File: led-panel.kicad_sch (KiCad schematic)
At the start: 0 parts

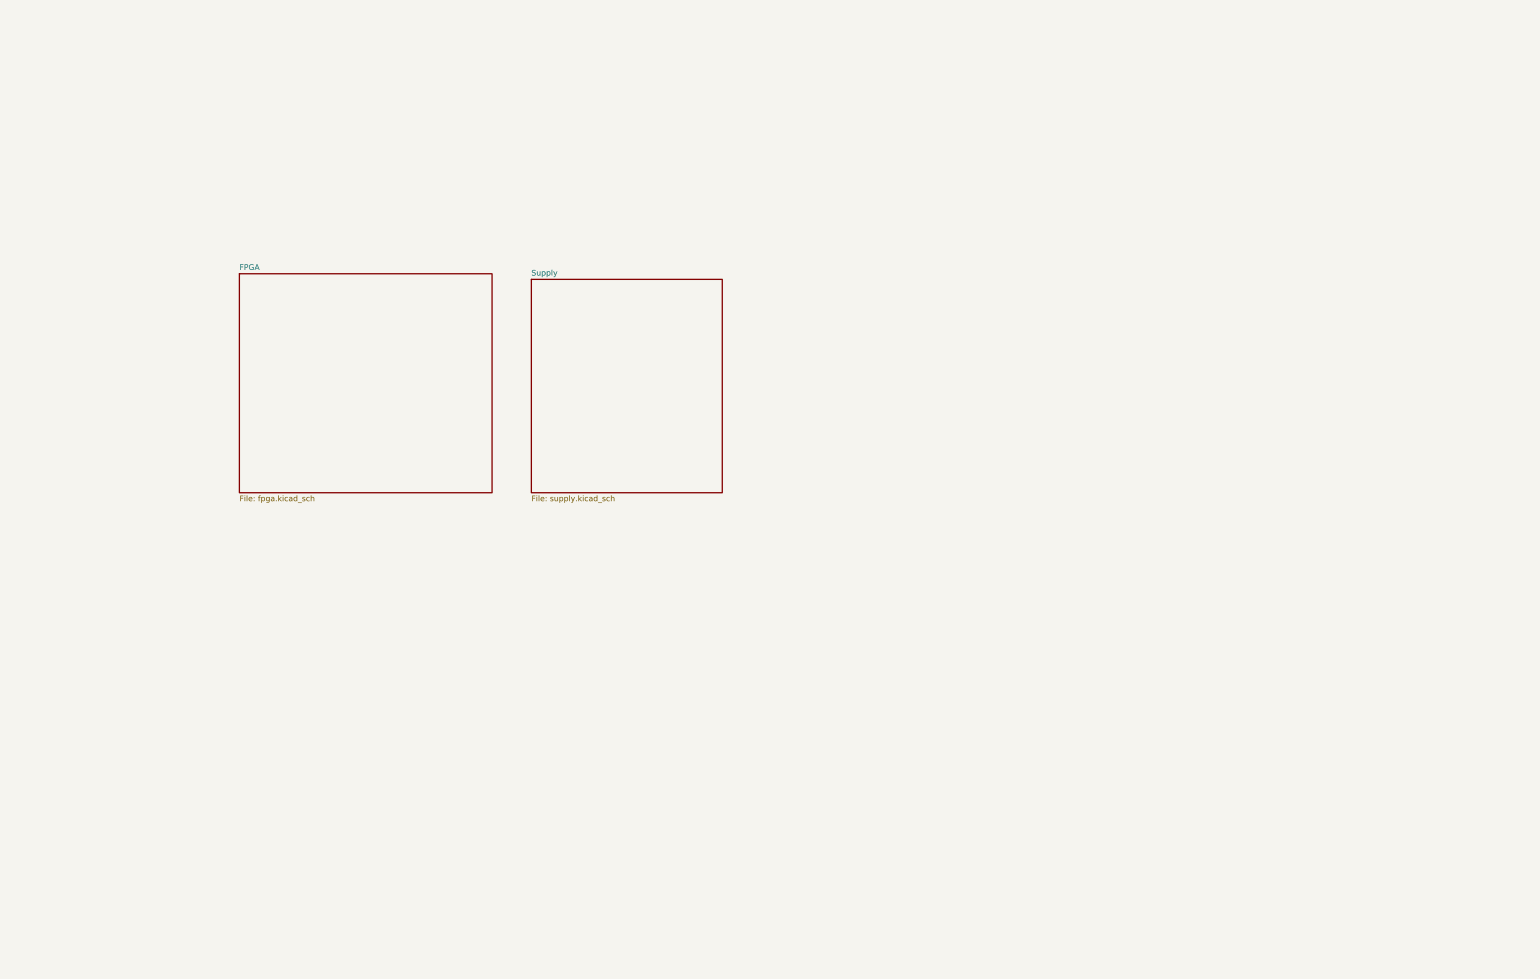
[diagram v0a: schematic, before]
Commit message: [#72133] Add rough schematic hierarchy
Signed-off-by: Dawid Lentka <dlentka@antmicro.com>
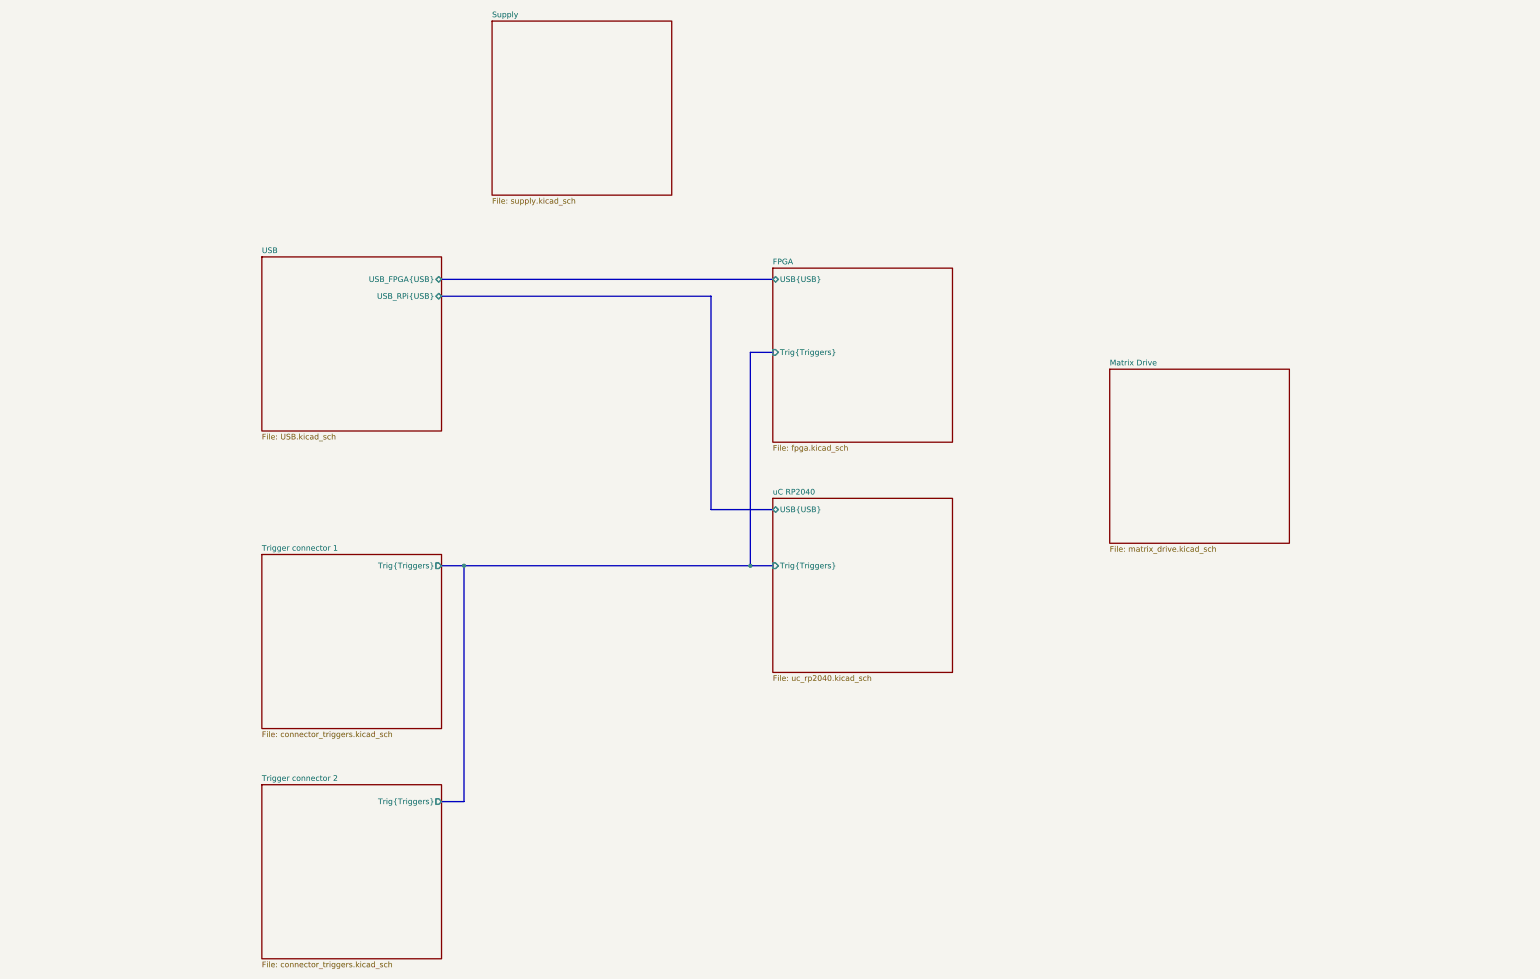
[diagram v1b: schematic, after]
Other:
- added sheet Matrix Drive (matrix_drive.kicad_sch)
- added sheet Trigger connector 1 (connector_triggers.kicad_sch)
- added sheet Trigger connector 2 (connector_triggers.kicad_sch)
- added sheet USB (USB.kicad_sch)
- added sheet uC RP2040 (uc_rp2040.kicad_sch)
- sheet FPGA ports: added Trig{Triggers}, USB{USB}; removed none

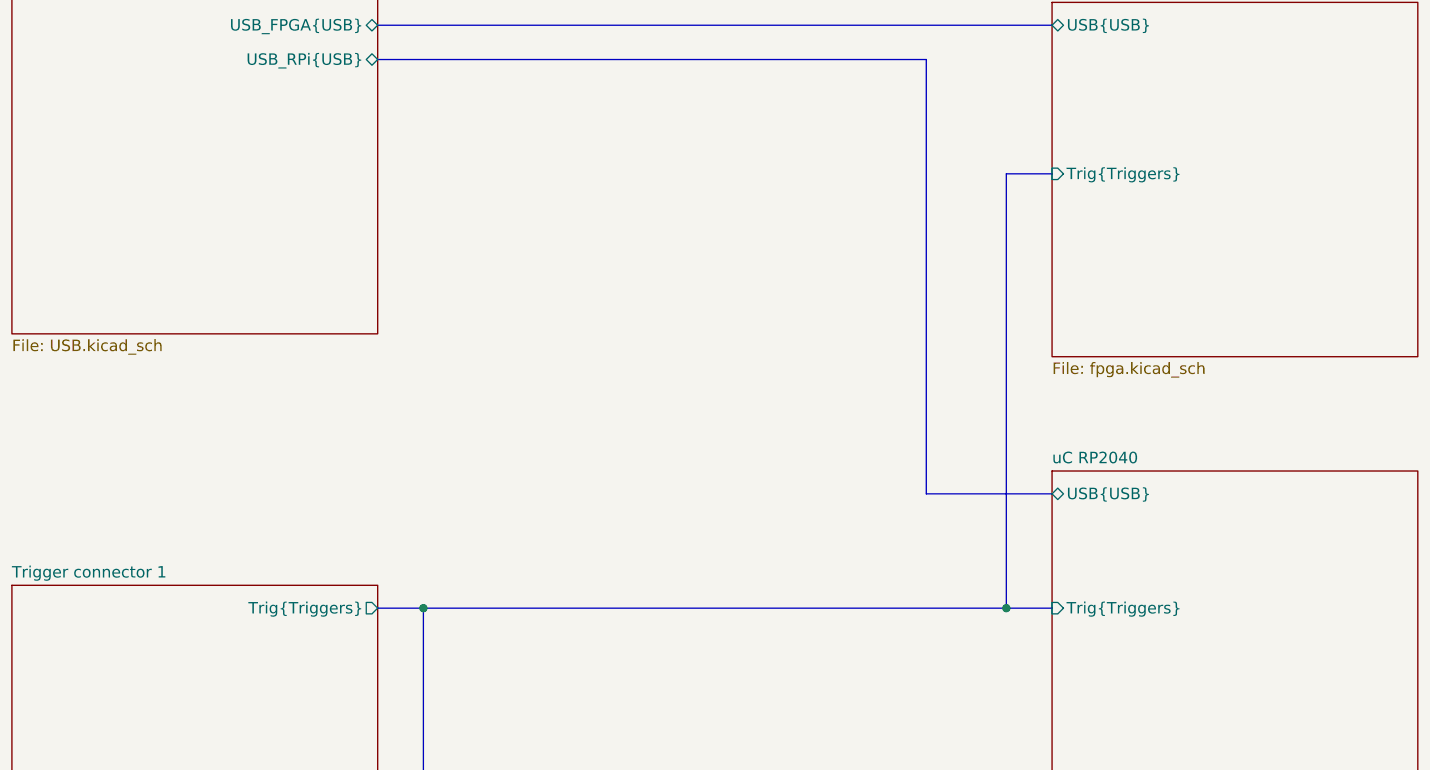
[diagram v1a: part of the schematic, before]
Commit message: [#72133] Add USB mux
Signed-off-by: Dawid Lentka <dlentka@antmicro.com>
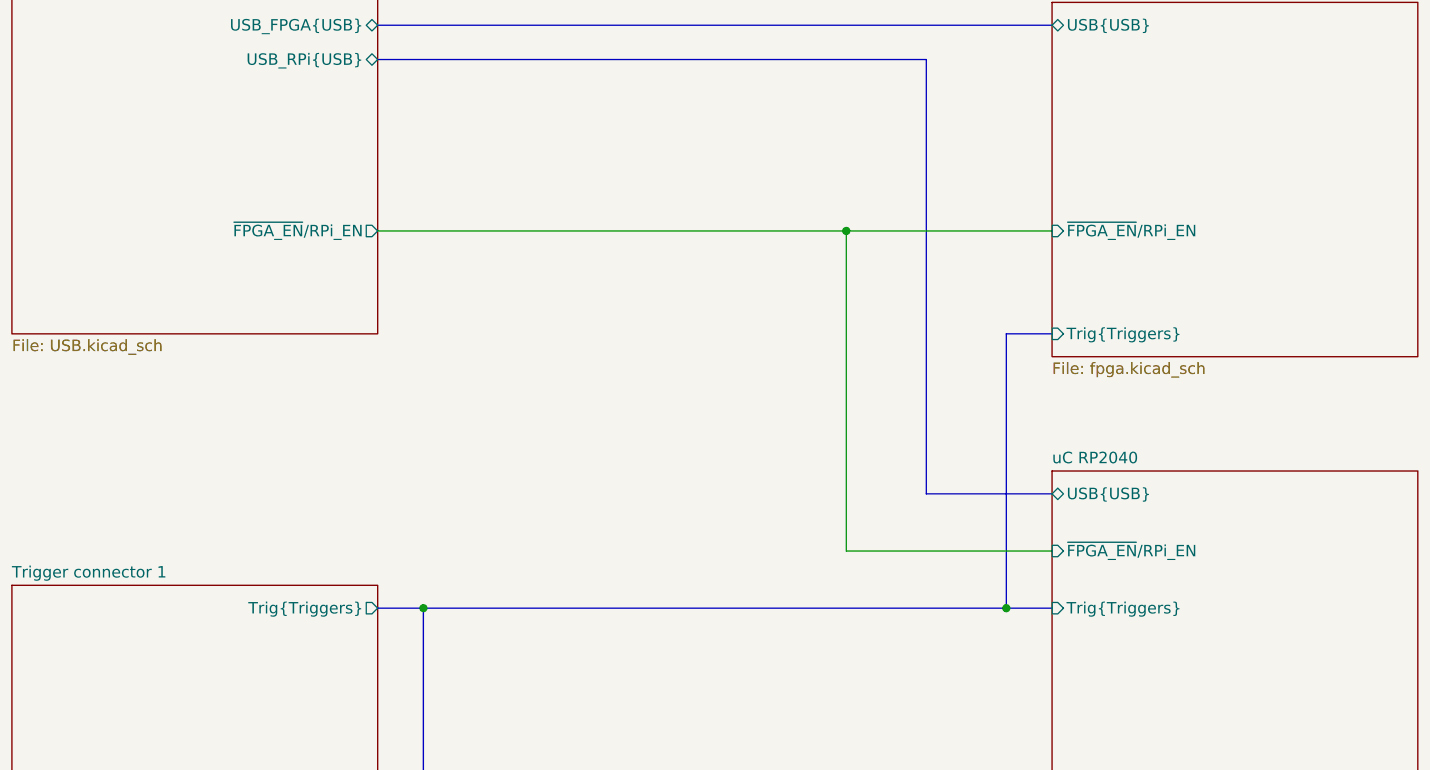
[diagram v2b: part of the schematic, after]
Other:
- sheet FPGA ports: added ~{FPGA_EN}/RPi_EN; removed none
- sheet USB ports: added ~{FPGA_EN}/RPi_EN; removed none
- sheet uC RP2040 ports: added ~{FPGA_EN}/RPi_EN; removed none
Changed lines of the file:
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@@
+	)
+	(junction
+		(at 171.45 99.06)
+		(diameter 0)
+		(color 0 0 0 0)
 	)
 	(junction
@@
 	(bus
 		(pts
-			(xy 189.23 92.71) (xy 189.23 140.97)
+			(xy 189.23 110.49) (xy 189.23 140.97)
 		)
 		(stroke
@@
 		)
 	)
+	(wire
+		(pts
+			(xy 171.45 99.06) (xy 194.31 99.06)
+		)
+		(stroke
+			(width 0)
+			(type default)
+		)
+	)
 	(bus
 		(pts
@@
 		)
 	)
-	(bus
-		(pts
-			(xy 194.31 92.71) (xy 189.23 92.71)
+	(wire
+		(pts
+			(xy 194.31 134.62) (xy 171.45 134.62)
+		)
+		(stroke
+			(width 0)
+			(type default)
+		)
+	)
+	(wire
+		(pts
+			(xy 171.45 134.62) (xy 171.45 99.06)
+		)
+		(stroke
+			(width 0)
+			(type default)
+		)
+	)
+	(bus
+		(pts
+			(xy 189.23 110.49) (xy 194.31 110.49)
 		)
 		(stroke
@@
 		(pts
 			(xy 189.23 140.97) (xy 194.31 140.97)
+		)
+		(stroke
+			(width 0)
+			(type default)
+		)
+	)
+	(wire
+		(pts
+			(xy 119.38 99.06) (xy 171.45 99.06)
 		)
 		(stroke
@@
 			)
 		)
+		(pin "~{FPGA_EN}{slash}RPi_EN" input
+			(at 194.31 134.62 180)
+			(effects
+				(font
+					(size 1.27 1.27)
+				)
+				(justify left)
+			)
+		)
 		(instances
 			(project "led-panel"
@@
 			)
 		)
+		(pin "~{FPGA_EN}{slash}RPi_EN" output
+			(at 119.38 99.06 0)
+			(effects
+				(font
+					(size 1.27 1.27)
+				)
+				(justify right)
+			)
+		)
 		(instances
 			(project "led-panel"
@@
 		)
 		(pin "Trig{Triggers}" input
-			(at 194.31 92.71 180)
+			(at 194.31 110.49 180)
 			(effects
 				(font
@@
 			(effects
 				(font
+					(size 1.27 1.27)
+				)
+				(justify left)
+			)
+		)
+		(pin "~{FPGA_EN}{slash}RPi_EN" input
+			(at 194.31 99.06 180)
+			(effects
+				(font

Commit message: [#72133] Add LED matrix
Signed-off-by: Dawid Lentka <dlentka@antmicro.com>
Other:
- added sheet Control (control.kicad_sch)
- added sheet Matrix High Side Drive (matrix_high_side_drive.kicad_sch)
- added sheet Matrix Low Side Drive (matrix_low_side_drive.kicad_sch)
- sheet FPGA ports: added 12MHz, ColumnCtrl[1..5], ColumnCtrl[6..10], RowCtrl[1..7], RowCtrl[8..14]; removed none
- sheet Matrix Drive ports: added ColumnDrive[1..5], ColumnDrive[6..10], RowDrive[1..7], RowDrive[8..14]; removed none
- sheet USB ports: added USB{USB}; removed USB_FPGA{USB}, USB_RPi{USB}, ~{FPGA_EN}/RPi_EN
- sheet uC RP2040 ports: added 12MHz, ColumnCtrl[1..5], ColumnCtrl[6..10], RowCtrl[1..7], RowCtrl[8..14]; removed none

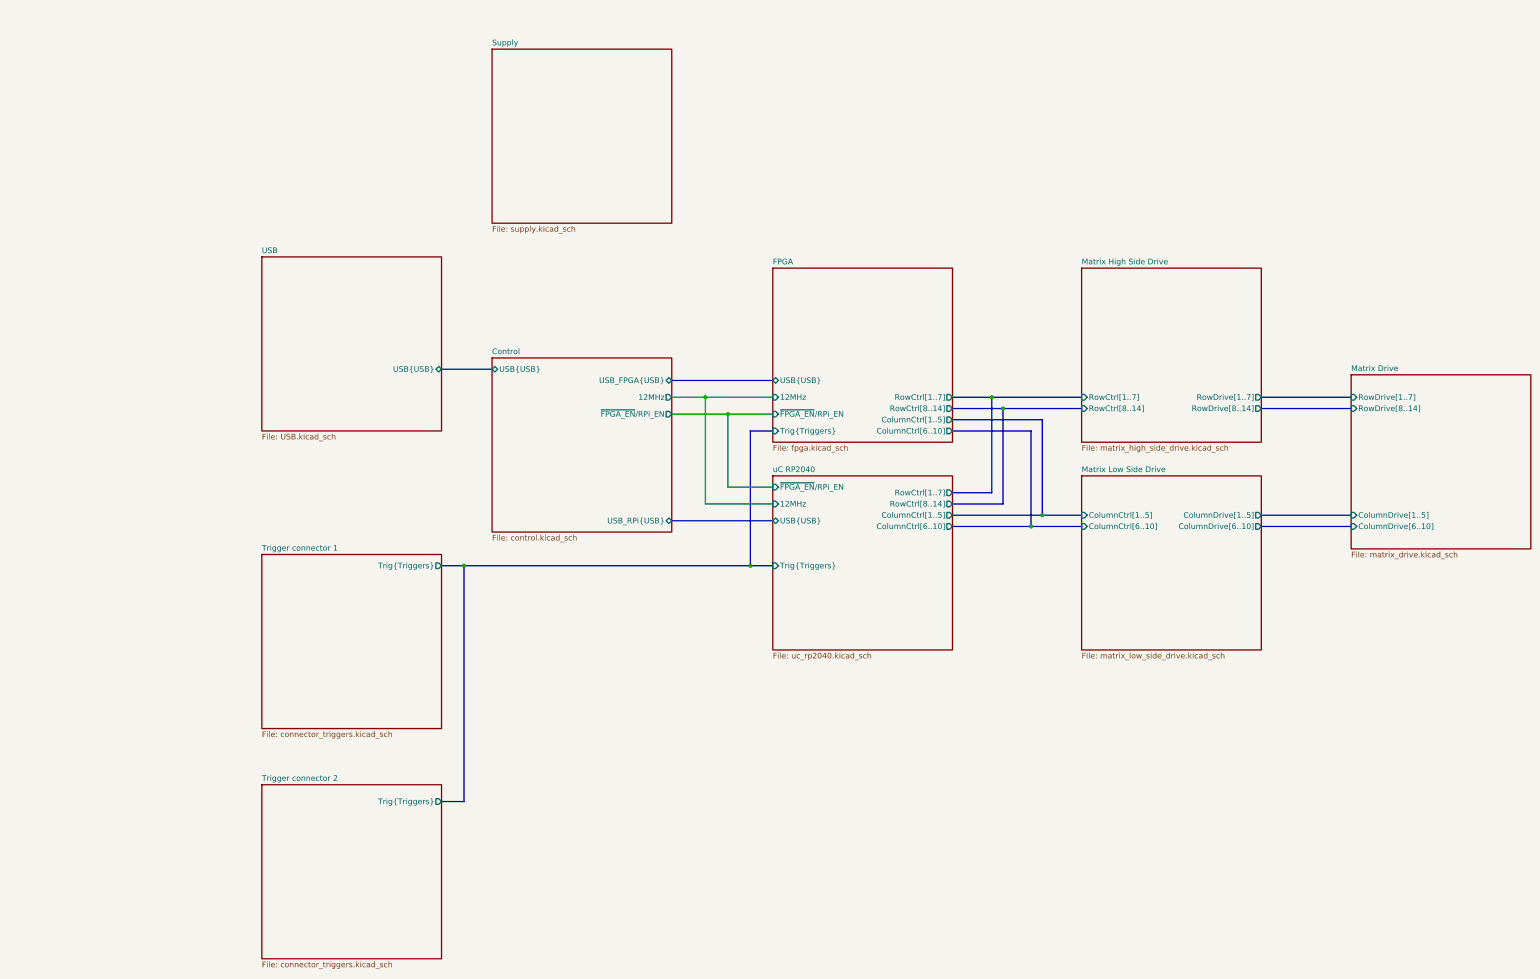
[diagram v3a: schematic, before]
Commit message: [#72133] Unify sheet size
Signed-off-by: Dawid Lentka <dlentka@antmicro.com>
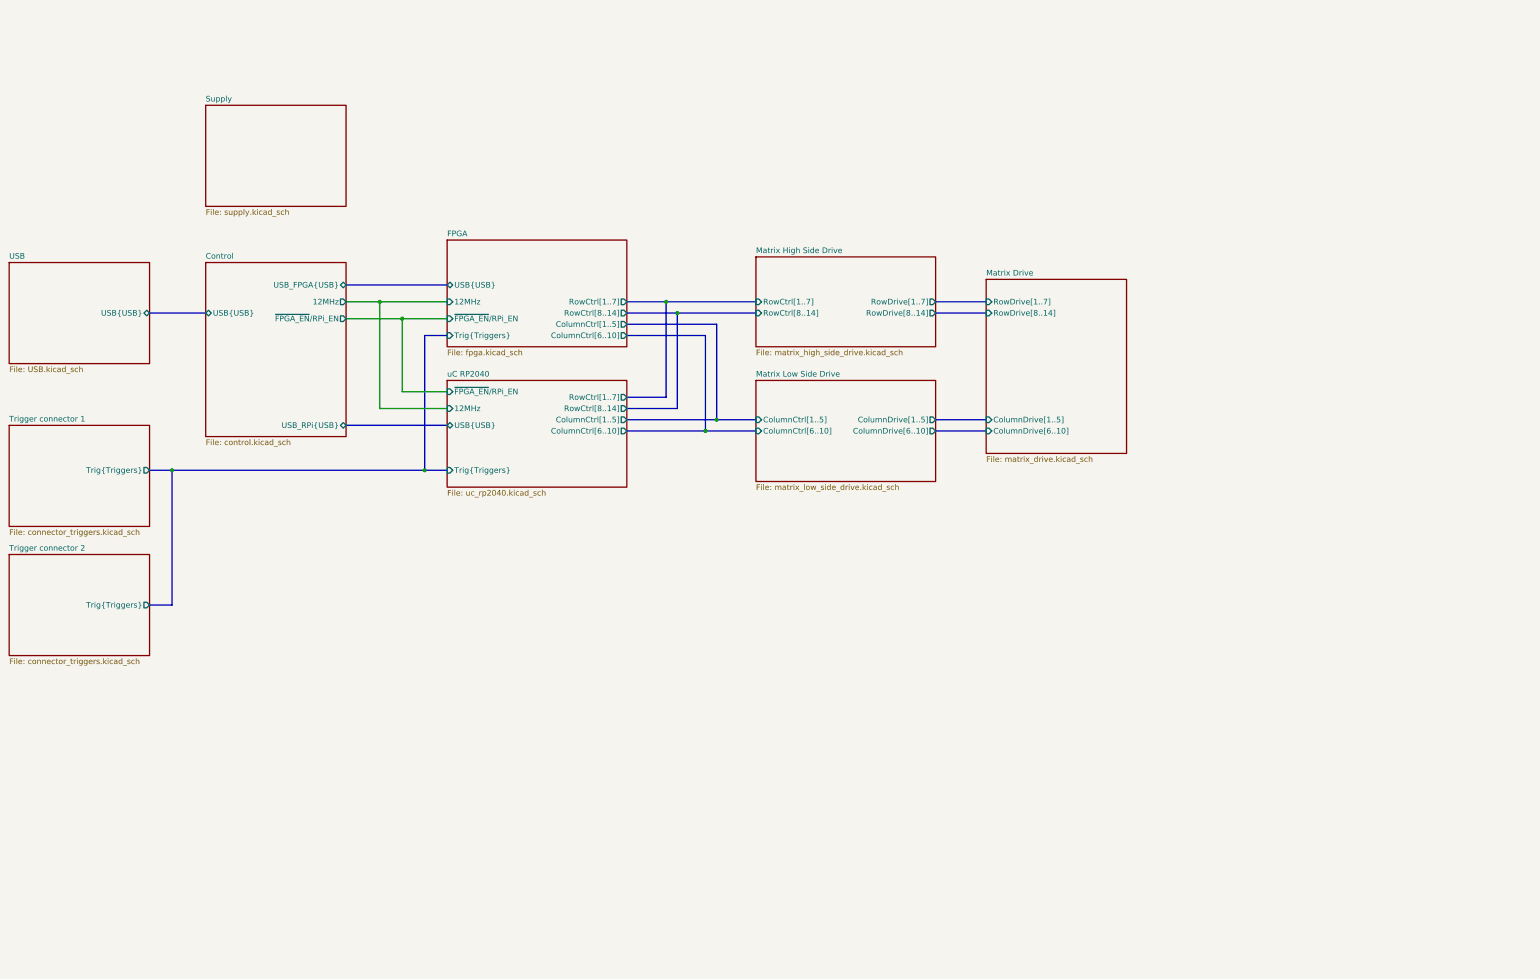
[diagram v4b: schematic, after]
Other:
- title: LED Panel -> LED Panel Board

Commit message: [#72133] Add mounting spacers
Signed-off-by: Dawid Lentka <dlentka@antmicro.com>
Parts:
- added H? (x4): Spacer_Drill5.4mm_H10mm_9774100482R, antmicro-footprints:Spacer_Drill5.4mm_H10mm_9774100482R, symbol antmicroMechanicalParts:Spacer_Drill5.4mm_H10mm_9774100482R
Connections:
- new net GND: H?.1, H?.1, H?.1, H?.1
